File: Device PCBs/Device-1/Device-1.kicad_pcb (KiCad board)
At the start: 2 copper layers, 55 x 55 mm, 34 parts, among them U1 EBYTE_E32-433T20D, U2 MAX487E

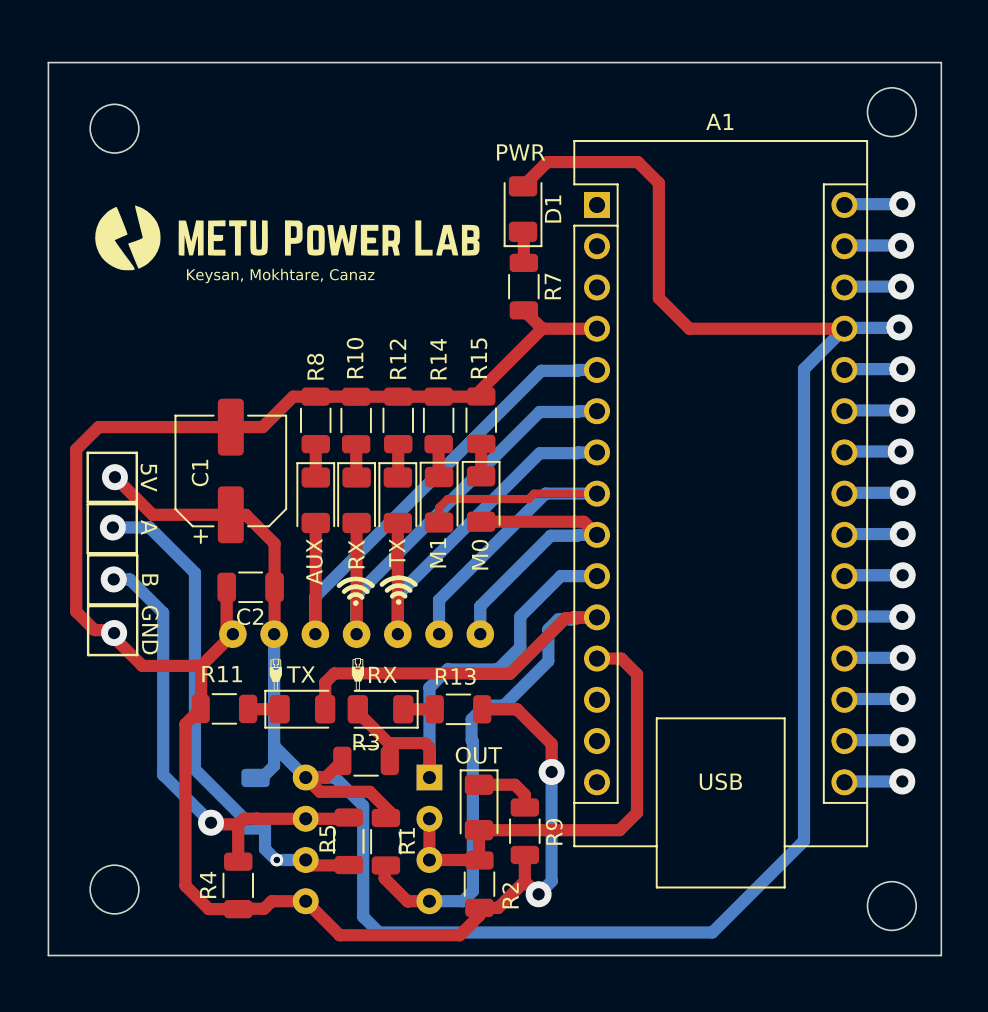
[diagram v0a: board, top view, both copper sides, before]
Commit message: slave config.h  and tescom_SDDPV2200M
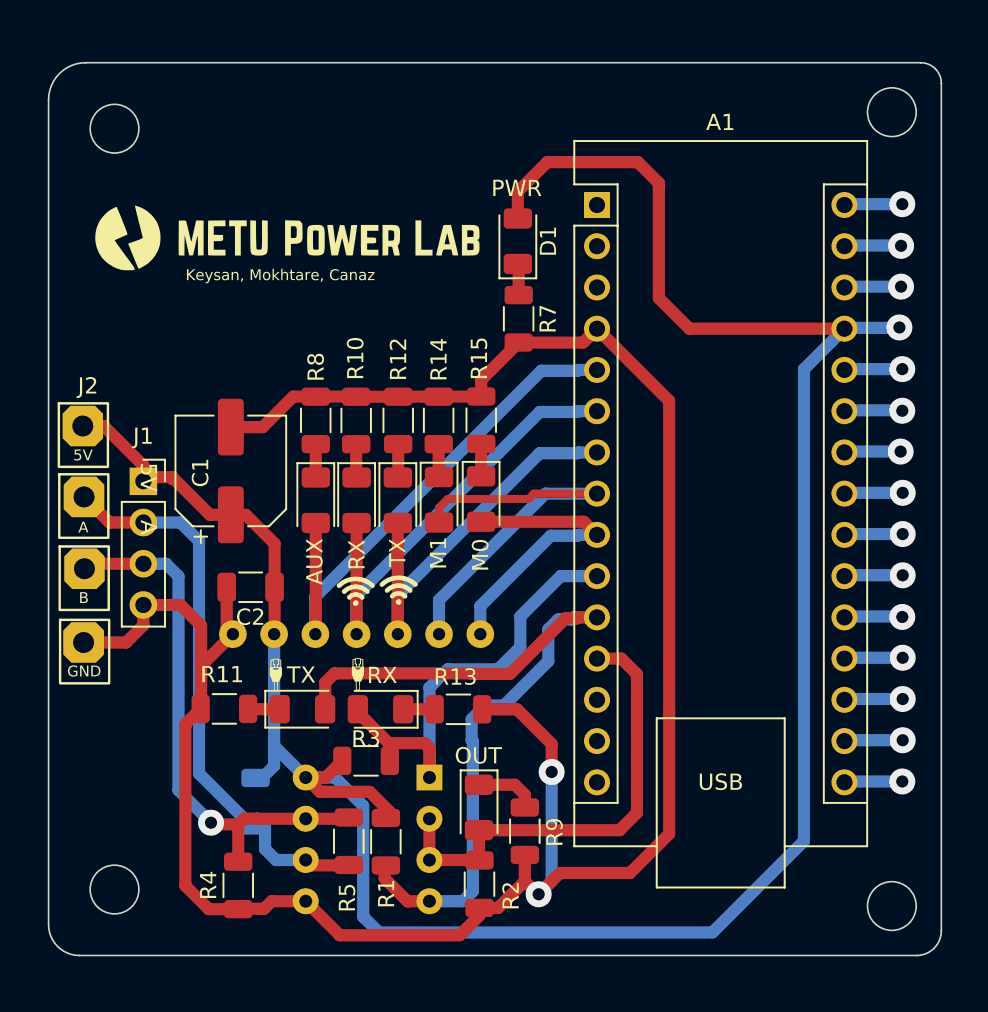
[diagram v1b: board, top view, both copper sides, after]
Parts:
- added J1: Conn_01x04_Female, Connector_PinSocket_2.54mm:PinSocket_1x04_P2.54mm_Vertical, F.Cu at (18.8, 38.7)
- added J2: Conn_01x04_Female, Device_1_project_footprints:output_vias, F.Cu at (15.0, 42.6)
- moved D1 2.01 mm to (41.9, 23.9)
- moved R7 2.01 mm to (41.9, 28.7)
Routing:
- net GND: track 117.8 -> 141.9 mm, vias 3 -> 2
- net 5V: track 145.3 -> 151.3 mm, vias 2 -> 1
- net B: track 29.3 -> 33.5 mm, vias 2 -> 1
- net A: track 30.7 -> 34.6 mm, vias 2 -> 0
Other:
- outline, holes or cut-outs redrawn
- board text removed: "B"
- board text removed: "GND"

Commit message: Device 1 PCB is finished
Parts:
- removed the G*** at (32.0, 50.6)
- removed the G*** at (26.9, 50.6)
- added ?: , , F.Cu at (15.9, 65.1)
- added ?: , , F.Cu at (15.8, 15.8)
- added ?: , , F.Cu at (65.0, 65.2)
- added G***: LOGO, LOGO, F.Cu at (40.5, 58.5)
- added G***: LOGO, LOGO, F.Cu at (40.5, 61.1)
- added REF**: MountingHole_3.2mm_M3_DIN965_Pad, MountingHole:MountingHole_3.2mm_M3_DIN965_Pad, F.Cu at (64.9, 15.9)
- added U10: signle_via, Device_1_project_footprints:single_via, F.Cu at (64.4, 52.3)
- added U11: signle_via, Device_1_project_footprints:single_via, F.Cu at (64.4, 49.7)
- added U12: signle_via, Device_1_project_footprints:single_via, F.Cu at (64.4, 47.1)
- added U13: signle_via, Device_1_project_footprints:single_via, F.Cu at (64.4, 44.6)
- added U14: signle_via, Device_1_project_footprints:single_via, F.Cu at (64.4, 42.0)
- added U15: signle_via, Device_1_project_footprints:single_via, F.Cu at (64.4, 39.5)
- added U16: signle_via, Device_1_project_footprints:single_via, F.Cu at (64.4, 36.9)
- added U17: signle_via, Device_1_project_footprints:single_via, F.Cu at (64.4, 34.4)
- added U18: signle_via, Device_1_project_footprints:single_via, F.Cu at (64.4, 31.8)
- added U19: signle_via, Device_1_project_footprints:single_via, F.Cu at (64.4, 21.6)
- added U20: signle_via, Device_1_project_footprints:single_via, F.Cu at (64.4, 29.2)
- added U21: signle_via, Device_1_project_footprints:single_via, F.Cu at (64.4, 54.9)
- added U22: signle_via, Device_1_project_footprints:single_via, F.Cu at (38.7, 16.2)
- added U23: signle_via, Device_1_project_footprints:single_via, F.Cu at (42.7, 16.2)
- added U3: signle_via, Device_1_project_footprints:single_via, F.Cu at (50.9, 65.2)
- added U4: signle_via, Device_1_project_footprints:single_via, F.Cu at (48.3, 65.2)
- added U5: signle_via, Device_1_project_footprints:single_via, F.Cu at (45.7, 65.2)
- added U6: signle_via, Device_1_project_footprints:single_via, F.Cu at (64.4, 57.5)
- added U7: signle_via, Device_1_project_footprints:single_via, F.Cu at (64.4, 24.2)
- added U8: signle_via, Device_1_project_footprints:single_via, F.Cu at (64.4, 26.7)
- added U9: signle_via, Device_1_project_footprints:single_via, F.Cu at (46.8, 16.2)
- C1: footprint Capacitor_SMD:CP_Elec_6.3x5.7 -> Capacitor_SMD:CP_Elec_6.3x5.2
- D1, D2, D3, D8, D9: footprint LED_SMD:LED_1206_3216Metric -> Device_1_project_footprints:lm281B-3000K
- D4, D5, D6, D7: footprint LED_SMD:LED_1206_3216Metric -> Device_1_project_footprints:lm281B-6500K
- R6: moved to F.Cu
- moved R2 16.1 mm to (23.4, 63.3), turned to 0 degrees
- moved R11 13.0 mm to (36.8, 53.7), turned to 90 degrees
- moved D5 10.9 mm to (37.6, 58.9)
- moved D7 9.98 mm to (37.6, 61.8), turned to 0 degrees
- moved R6 7.72 mm to (26.3, 50.8), turned to 0 degrees
- moved R4 7.57 mm to (22.3, 56.4), turned to -90 degrees
- moved U2 7.49 mm to (30.0, 60.8), turned to 90 degrees
- moved R5 7.47 mm to (26.0, 55.8), turned to 180 degrees
- moved J1 7.30 mm to (19.3, 46.0), turned to 180 degrees
- moved R9 6.63 mm to (41.7, 53.7), turned to 90 degrees
- moved D3 5.60 mm to (37.3, 64.0), turned to 0 degrees
- moved R1 4.11 mm to (32.8, 56.9)
- moved R12 2.84 mm to (34.4, 32.1)
- moved R14 2.84 mm to (36.9, 32.1)
- moved R15 2.84 mm to (39.5, 32.1)
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- renumbered A1 to ArduinoNano1
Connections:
- ArduinoNano1 pad 1: unconnected-(A1-Pad1) -> Net-(ArduinoNano1-Pad1)
- ArduinoNano1 pad 13: unconnected-(A1-Pad13) -> Net-(ArduinoNano1-Pad13)
- ArduinoNano1 pad 14: unconnected-(A1-Pad14) -> Net-(ArduinoNano1-Pad14)
- ArduinoNano1 pad 15: unconnected-(A1-Pad15) -> Net-(ArduinoNano1-Pad15)
- ArduinoNano1 pad 16: unconnected-(A1-Pad16) -> Net-(ArduinoNano1-Pad16)
- ArduinoNano1 pad 17: unconnected-(A1-Pad17) -> Net-(ArduinoNano1-Pad17)
- ArduinoNano1 pad 18: unconnected-(A1-Pad18) -> Net-(ArduinoNano1-Pad18)
- ArduinoNano1 pad 19: unconnected-(A1-Pad19) -> Net-(ArduinoNano1-Pad19)
- ArduinoNano1 pad 2: unconnected-(A1-Pad2) -> Net-(ArduinoNano1-Pad2)
- ArduinoNano1 pad 20: unconnected-(A1-Pad20) -> Net-(ArduinoNano1-Pad20)
- ArduinoNano1 pad 21: unconnected-(A1-Pad21) -> Net-(ArduinoNano1-Pad21)
- ArduinoNano1 pad 22: unconnected-(A1-Pad22) -> Net-(ArduinoNano1-Pad22)
- ArduinoNano1 pad 23: unconnected-(A1-Pad23) -> Net-(ArduinoNano1-Pad23)
- ArduinoNano1 pad 24: unconnected-(A1-Pad24) -> Net-(ArduinoNano1-Pad24)
- ArduinoNano1 pad 25: unconnected-(A1-Pad25) -> Net-(ArduinoNano1-Pad25)
- ArduinoNano1 pad 26: unconnected-(A1-Pad26) -> Net-(ArduinoNano1-Pad26)
- ArduinoNano1 pad 28: unconnected-(A1-Pad28) -> Net-(ArduinoNano1-Pad28)
- ArduinoNano1 pad 29: unconnected-(A1-Pad29) -> Net-(ArduinoNano1-Pad29)
- ArduinoNano1 pad 3: unconnected-(A1-Pad3) -> Net-(ArduinoNano1-Pad3)
- ArduinoNano1 pad 30: unconnected-(A1-Pad30) -> Net-(ArduinoNano1-Pad30)
- J1 pad 1: 5V -> B
- J1 pad 3: B -> GND
- J1 pad 4: GND -> 5V
- J2 pad 1: GND -> B
- J2 pad 2: B -> A
- J2 pad 3: A -> GND
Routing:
- net 5V: track 151.3 -> 97.7 mm, vias 1 -> 0
- net GND: track 141.9 -> 102.9 mm, vias 2 -> 3
- net Net-(ArduinoNano1-Pad13): track 0.00 -> 16.3 mm
- net Net-(ArduinoNano1-Pad3): track 0.00 -> 14.9 mm
- net Net-(ArduinoNano1-Pad2): track 0.00 -> 14.4 mm
- net Net-(ArduinoNano1-Pad14): track 0.00 -> 12.2 mm
- net RS485_OUTPUT_ENABLE_PIN: track 29.1 -> 40.2 mm, vias 0 -> 1
- net Net-(ArduinoNano1-Pad1): track 0.00 -> 11.0 mm
- net Net-(ArduinoNano1-Pad15): track 0.00 -> 8.44 mm
- net RS485_SS_TX_PIN: track 49.3 -> 40.9 mm, vias 0 -> 1
- net M1: track 25.6 -> 18.1 mm, vias 0 -> 1
- net A: track 34.6 -> 27.3 mm
- net RS485_SS_RX_PIN: track 28.3 -> 35.4 mm, vias 0 -> 1
- net Net-(D3-Pad1): track 4.07 -> 11.1 mm
- net Net-(D7-Pad1): track 1.94 -> 8.18 mm
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- added copper zone on B.Cu, net GND
- added copper zone on F.Cu, net GND
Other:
- outline, holes or cut-outs redrawn
- board text added: "100nF"
- board text added: "10k"
- board text added: "120"
- board text added: "20k"
- board text added: "3.3k"
- board text added: "3V3"
- board text added: "47uF"
- board text added: "A0"
- board text added: "A1"
- board text added: "A2"
- board text added: "A3"
- board text added: "A4"
- board text added: "A5"
- board text added: "A6"
- board text added: "A7"
- board text added: "AREF"
- board text added: "D10"
- board text added: "D11"
- board text added: "D12"
- board text added: "D13"
- board text added: "D2"
- board text added: "D3"
- board text added: "D4"
- board text added: "D5"
- board text added: "D6"
- board text added: "Designed by Erdem Canaz 27.02.2023 github.com/erdemcanaz"
- board text added: "EBYTE-E32"
- board text added: "GND"
- board text added: "MAX487"
- board text added: "PWR-"
- board text added: "RX/D0"
- board text added: "TX/D1"
- board text added: "Vin"
- board text added: "~RST"
- board text removed: "PWR"

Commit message: PCB and slave fix
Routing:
- net Net-(ArduinoNano1-Pad17): track 4.25 -> 8.18 mm
- net Net-(ArduinoNano1-Pad16): track 4.32 -> 8.25 mm
- net Net-(ArduinoNano1-Pad18): track 3.27 -> 7.19 mm
- net Net-(ArduinoNano1-Pad19): track 3.26 -> 7.14 mm
- net Net-(ArduinoNano1-Pad22): track 3.26 -> 7.14 mm
- net Net-(ArduinoNano1-Pad26): track 3.08 -> 6.94 mm
- net Net-(ArduinoNano1-Pad25): track 3.22 -> 7.06 mm
- net Net-(ArduinoNano1-Pad24): track 3.22 -> 7.06 mm
- net Net-(ArduinoNano1-Pad23): track 3.22 -> 7.06 mm
- net Net-(ArduinoNano1-Pad21): track 3.22 -> 7.06 mm
- net Net-(ArduinoNano1-Pad20): track 3.22 -> 7.06 mm
- net Net-(ArduinoNano1-Pad29): track 3.10 -> 6.94 mm
- net Net-(ArduinoNano1-Pad30): track 3.10 -> 6.94 mm
- net 5V: track 97.7 -> 101.5 mm
- net Net-(ArduinoNano1-Pad28): track 3.08 -> 6.88 mm
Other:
- board text removed: "100nF"
- board text removed: "10k"
- board text removed: "120"
- board text removed: "20k"
- board text removed: "3.3k"
- board text removed: "47uF"
- board text removed: "A"

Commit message: PCBway gerbers are finished.
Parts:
- added R16: 3.3k, Resistor_SMD:R_1206_3216Metric, F.Cu at (35.6, 44.9)
- added R17: 3.3k, Resistor_SMD:R_1206_3216Metric, F.Cu at (38.6, 45.0)
- added R18: 3.3k, Resistor_SMD:R_1206_3216Metric, F.Cu at (41.7, 45.1)
- moved G*** 0.78 mm to (32.1, 42.7)
- moved G*** 0.64 mm to (35.2, 42.7)
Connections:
- ArduinoNano1 pad 7: EBYTE_RX -> Net-(ArduinoNano1-Pad7)
- ArduinoNano1 pad 8: M1 -> Net-(ArduinoNano1-Pad8)
- ArduinoNano1 pad 9: M0 -> Net-(ArduinoNano1-Pad9)
- D6 pad 2: EBYTE_RX -> Net-(ArduinoNano1-Pad7)
- D8 pad 2: M1 -> Net-(ArduinoNano1-Pad8)
- D9 pad 2: M0 -> Net-(ArduinoNano1-Pad9)
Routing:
- net EBYTE_RX: track 22.2 -> 2.32 mm, vias 1 -> 0
- net Net-(ArduinoNano1-Pad7): track 0.00 -> 17.4 mm, vias 0 -> 1
- net M1: track 18.2 -> 2.46 mm, vias 1 -> 0
- net M0: track 14.6 -> 2.64 mm, vias 1 -> 0
- net Net-(ArduinoNano1-Pad8): track 0.00 -> 11.8 mm, vias 0 -> 1
- net Net-(ArduinoNano1-Pad9): track 0.00 -> 9.76 mm
- net RS485_SS_RX_PIN: track 35.4 -> 34.2 mm
- net RS485_OUTPUT_ENABLE_PIN: track 40.2 -> 39.0 mm
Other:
- board text added: "PWR"
- board text removed: "PWR-"
